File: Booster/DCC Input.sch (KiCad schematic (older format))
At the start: 17 parts, among them P201 CONN_01X02, P202 CONN_01X02, SW201 FORCE_ENABLE, U201 6N136, U203 LM339, Y701 74HC86

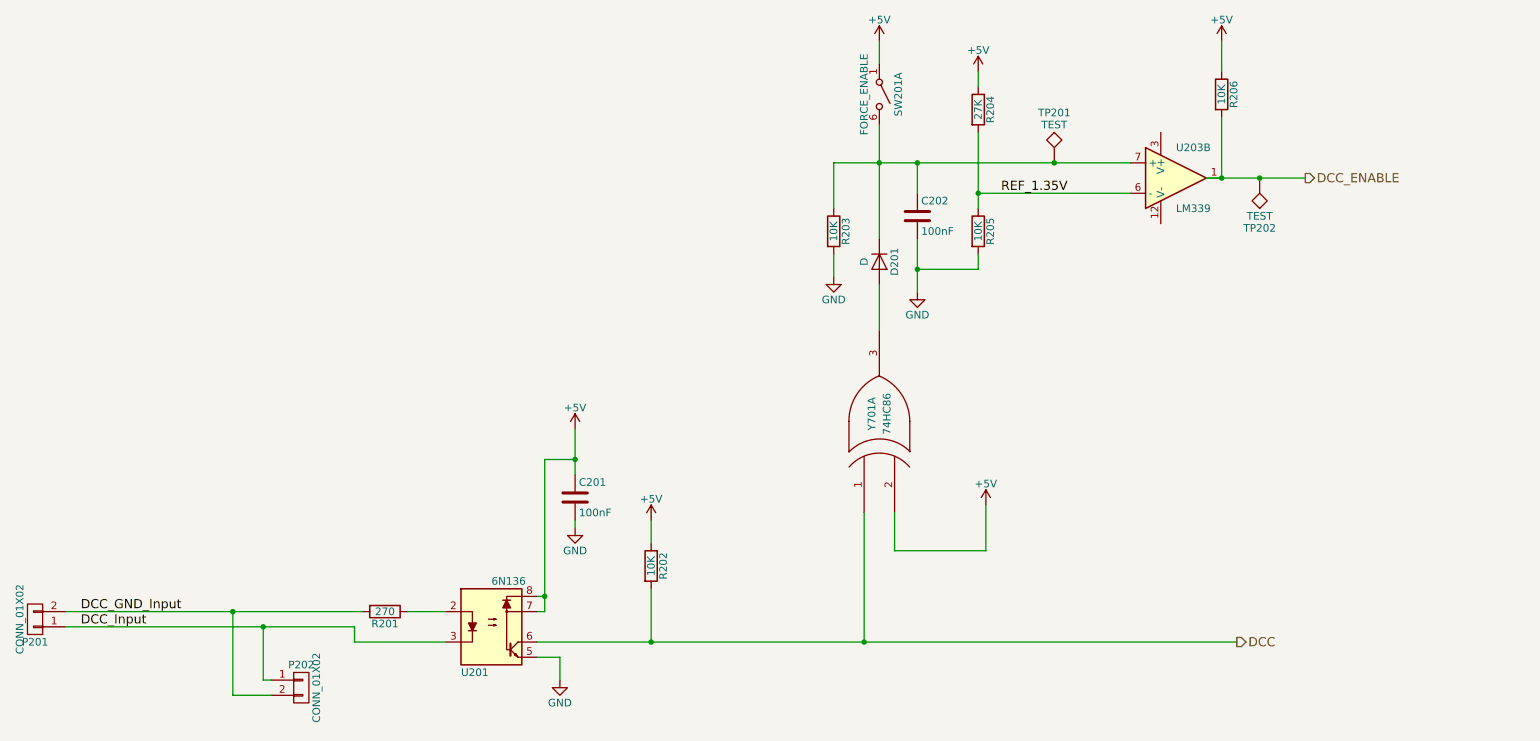
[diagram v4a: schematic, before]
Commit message: Assigned footprints & minor adjustments.
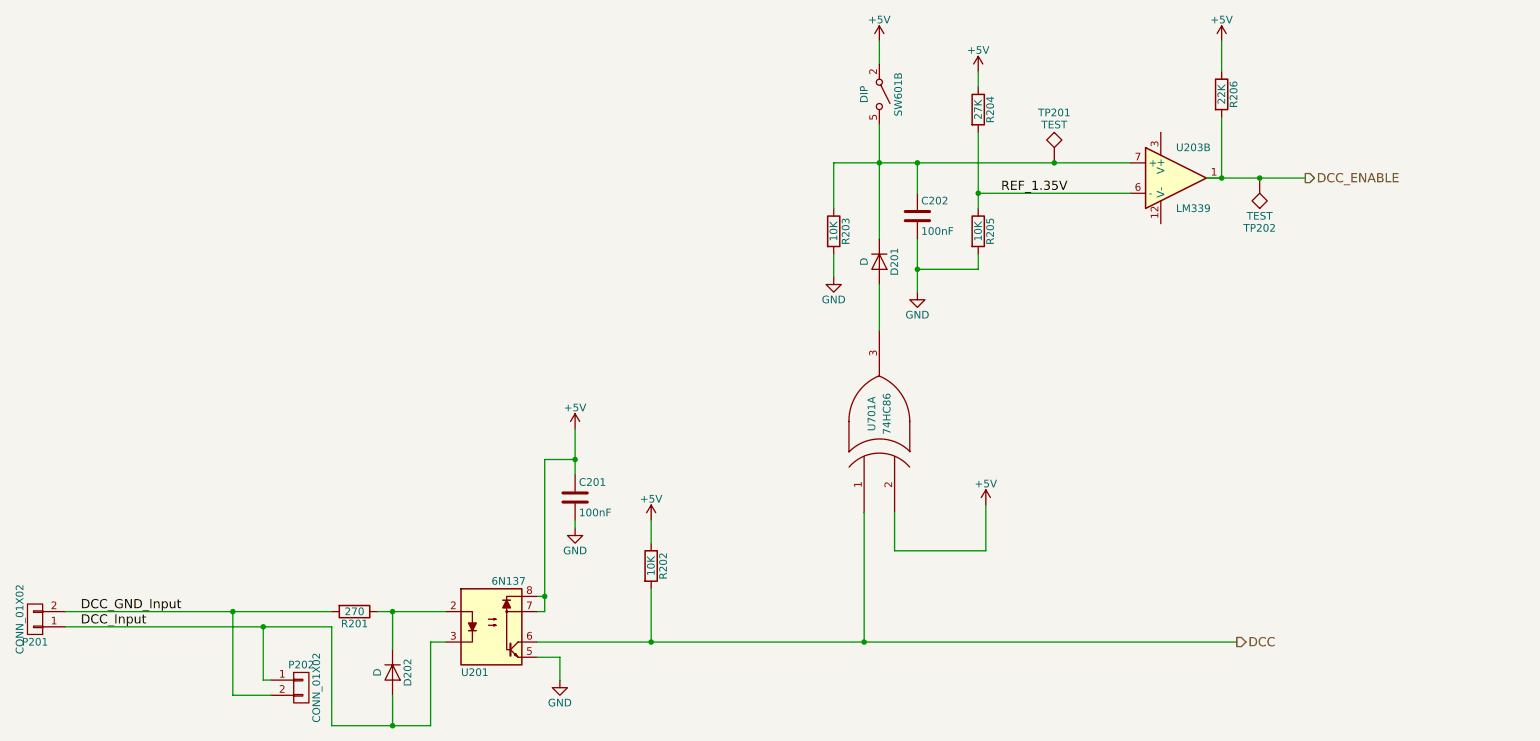
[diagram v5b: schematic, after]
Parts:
- added D202: D, Diodes_SMD:D_MiniMELF, symbol D
- C201, C202: footprint (none) -> Capacitors_SMD:C_0805
- D201: footprint (none) -> Diodes_SMD:D_MiniMELF
- P201, P202: footprint (none) -> Connectors_JST:JST_XH_B02B-XH-A_02x2.50mm_Straight
- R201, R202, R203, R204, R205: footprint (none) -> Resistors_SMD:R_0805
- R206: value 10K -> 22K; footprint (none) -> Resistors_SMD:R_0805
- SW601: renamed from SW201; value FORCE_ENABLE -> DIP; footprint (none) -> Buttons_Switches_THT:SW_DIP_x3_W7.62mm_Slide
- TP201, TP202: footprint (none) -> Measurement_Points:Measurement_Point_Round-TH_Small
- U201: value 6N136 -> 6N137
- U203: footprint (none) -> SMD_Packages:SOIC-14_N
- U701: renamed from Y701; footprint (none) -> SMD_Packages:SOIC-14_N
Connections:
- net +5V: now also SW601.2 (A); no longer SW601.1 (A)
- net DCC_Input: now also D202.2 (A)
- net at R201.1, U201.2: now also D202.1 (K)
- net at C202.1, D201.1 (K), R203.1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: now also SW601.5 (B); no longer SW601.6 (B)
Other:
- moved on the sheet: R201
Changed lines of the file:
@@
 P 4350 4900
 F 0 "U201" H 4150 4600 50  0000 L CNN
-F 1 "6N136" H 4350 5200 50  0000 L CNN
+F 1 "6N137" H 4350 5200 50  0000 L CNN
 F 2 "Housings_DIP:DIP-8_W7.62mm" H 4150 4600 50  0001 L CIN
 F 3 "" H 4350 4900 50  0001 L CNN
@@
 L R R201
 U 1 1 59E8F235
-P 3650 4800
-F 0 "R201" V 3730 4800 50  0000 C CNN
-F 1 "270" V 3650 4800 50  0000 C CNN
-F 2 "" V 3580 4800 50  0001 C CNN
-F 3 "" H 3650 4800 50  0001 C CNN
-	1    3650 4800
+P 3450 4800
+F 0 "R201" V 3530 4800 50  0000 C CNN
+F 1 "270" V 3450 4800 50  0000 C CNN
+F 2 "Resistors_SMD:R_0805" V 3380 4800 50  0001 C CNN
+F 3 "" H 3450 4800 50  0001 C CNN
+	1    3450 4800
 	0    1    1    0
 $EndComp
@@
 F 0 "C201" H 4925 4150 50  0000 L CNN
 F 1 "100nF" H 4925 3950 50  0000 L CNN
-F 2 "" H 4938 3900 50  0001 C CNN
+F 2 "Capacitors_SMD:C_0805" H 4938 3900 50  0001 C CNN
 F 3 "" H 4900 4050 50  0001 C CNN
 	1    4900 4050
@@
 F 0 "R202" V 5480 4500 50  0000 C CNN
 F 1 "10K" V 5400 4500 50  0000 C CNN
-F 2 "" V 5330 4500 50  0001 C CNN
+F 2 "Resistors_SMD:R_0805" V 5330 4500 50  0001 C CNN
 F 3 "" H 5400 4500 50  0001 C CNN
 	1    5400 4500
@@
 F 0 "D201" H 6900 2600 50  0000 C CNN
 F 1 "D" H 6900 2400 50  0000 C CNN
-F 2 "" H 6900 2500 50  0000 C CNN
+F 2 "Diodes_SMD:D_MiniMELF" H 6900 2500 50  0001 C CNN
 F 3 "" H 6900 2500 50  0000 C CNN
 	1    6900 2500
@@
 F 0 "C202" H 7175 2300 50  0000 L CNN
 F 1 "100nF" H 7175 2100 50  0000 L CNN
-F 2 "" H 7188 2050 50  0000 C CNN
+F 2 "Capacitors_SMD:C_0805" H 7188 2050 50  0001 C CNN
 F 3 "" H 7150 2200 50  0000 C CNN
 	1    7150 2200
@@
 F 0 "U203" H 8850 2150 50  0000 L CNN
 F 1 "LM339" H 8850 1750 50  0000 L CNN
-F 2 "" H 8800 2050 50  0000 C CNN
+F 2 "SMD_Packages:SOIC-14_N" H 8800 2050 50  0001 C CNN
 F 3 "" H 8900 2150 50  0000 C CNN
 	2    8850 1950
@@
 F 0 "R204" V 7630 1500 50  0000 C CNN
 F 1 "27K" V 7550 1500 50  0000 C CNN
-F 2 "" V 7480 1500 50  0000 C CNN
+F 2 "Resistors_SMD:R_0805" V 7480 1500 50  0001 C CNN
 F 3 "" H 7550 1500 50  0000 C CNN
 	1    7550 1500
@@
 F 0 "R205" V 7630 2300 50  0000 C CNN
 F 1 "10K" V 7550 2300 50  0000 C CNN
-F 2 "" V 7480 2300 50  0000 C CNN
+F 2 "Resistors_SMD:R_0805" V 7480 2300 50  0001 C CNN
 F 3 "" H 7550 2300 50  0000 C CNN
 	1    7550 2300
@@
 F 0 "R203" V 6680 2300 50  0000 C CNN
 F 1 "10K" V 6600 2300 50  0000 C CNN
-F 2 "" V 6530 2300 50  0000 C CNN
+F 2 "Resistors_SMD:R_0805" V 6530 2300 50  0001 C CNN
 F 3 "" H 6600 2300 50  0000 C CNN
 	1    6600 2300
@@
 P 9150 1400
 F 0 "R206" V 9230 1400 50  0000 C CNN
-F 1 "10K" V 9150 1400 50  0000 C CNN
-F 2 "" V 9080 1400 50  0000 C CNN
+F 1 "22K" V 9150 1400 50  0000 C CNN
+F 2 "Resistors_SMD:R_0805" V 9080 1400 50  0001 C CNN
 F 3 "" H 9150 1400 50  0000 C CNN
 	1    9150 1400
@@
 REF_1.35V
 $Comp
-L SW_SPST_x03 SW201
-U 1 1 5A38F800
+L SW_SPST_x03 SW601
+U 2 1 5A38F800
 P 6900 1400
-F 0 "SW201" H 6900 1525 50  0000 C CNN
-F 1 "FORCE_ENABLE" H 6900 1300 50  0000 C CNN
-F 2 "" H 6900 1400 50  0001 C CNN
+F 0 "SW601" H 6900 1525 50  0000 C CNN
+F 1 "DIP" H 6900 1300 50  0000 C CNN
+F 2 "Buttons_Switches_THT:SW_DIP_x3_W7.62mm_Slide" H 6900 1400 50  0001 C CNN
 F 3 "" H 6900 1400 50  0001 C CNN
-	1    6900 1400
+	2    6900 1400
 	0    1    1    0
 $EndComp
@@
 F 0 "P202" H 3100 5450 50  0000 C CNN
 F 1 "CONN_01X02" V 3200 5300 50  0000 C CNN
-F 2 "" H 3100 5300 50  0000 C CNN
+F 2 "Connectors_JST:JST_XH_B02B-XH-A_02x2.50mm_Straight" H 3100 5300 50  0001 C CNN
 F 3 "" H 3100 5300 50  0000 C CNN
 	1    3100 5300
@@
 F 0 "P201" H 1350 5000 50  0000 C CNN
 F 1 "CONN_01X02" V 1450 4850 50  0000 C CNN
-F 2 "" H 1350 4850 50  0000 C CNN
+F 2 "Connectors_JST:JST_XH_B02B-XH-A_02x2.50mm_Straight" H 1350 4850 50  0001 C CNN
 F 3 "" H 1350 4850 50  0000 C CNN
 	1    1350 4850
@@
 $EndComp
 $Comp
-L 74HC86 Y701
+L 74HC86 U701
 U 1 1 5A3AC211
 P 6900 3550
-F 0 "Y701" H 6950 3600 50  0000 C CNN
+F 0 "U701" H 6950 3600 50  0000 C CNN
 F 1 "74HC86" H 6950 3500 50  0000 C CNN
-F 2 "" H 6900 3550 50  0000 C CNN
+F 2 "SMD_Packages:SOIC-14_N" H 6900 3550 50  0001 C CNN
 F 3 "" H 6900 3550 50  0000 C CNN
 	1    6900 3550
@@
 F 0 "TP202" H 9400 2250 50  0000 C BNN
 F 1 "TEST" H 9400 2200 50  0000 C CNN
-F 2 "" H 9400 1950 50  0000 C CNN
+F 2 "Measurement_Points:Measurement_Point_Round-TH_Small" H 9400 1950 50  0001 C CNN
 F 3 "" H 9400 1950 50  0000 C CNN
 	1    9400 1950
@@
 F 0 "TP201" H 8050 2150 50  0000 C BNN
 F 1 "TEST" H 8050 2100 50  0000 C CNN
-F 2 "" H 8050 1850 50  0000 C CNN
+F 2 "Measurement_Points:Measurement_Point_Round-TH_Small" H 8050 1850 50  0001 C CNN
 F 3 "" H 8050 1850 50  0000 C CNN
 	1    8050 1850
@@
 	6900 2950 6900 2650
 Wire Wire Line
-	6800 4150 6800 5000
-Wire Wire Line
-	3800 4800 4050 4800
-Wire Wire Line
-	3450 5000 4050 5000
+	6800 5000 6800 4150
+Wire Wire Line
+	3600 4800 4050 4800
 Wire Wire Line
 	5400 4350 5400 4200
@@
 	7550 2450 7550 2550
 Wire Wire Line
-	3450 4900 3450 5000
+	3300 4900 3300 5550
 Connection ~ 6800 5000
 Connection ~ 7150 1850
@@
 	2900 5250 2850 5250
 Wire Wire Line
-	1550 4900 3450 4900
-Wire Wire Line
-	1550 4800 3500 4800
+	1550 4900 3300 4900
+Wire Wire Line
+	1550 4800 3300 4800
+$Comp
+L D D202
+U 1 1 5A411C39
+P 3700 5200
+F 0 "D202" H 3700 5300 50  0000 C CNN
+F 1 "D" H 3700 5100 50  0000 C CNN
+F 2 "Diodes_SMD:D_MiniMELF" H 3700 5200 50  0001 C CNN
+F 3 "" H 3700 5200 50  0000 C CNN
+	1    3700 5200
+	0    1    1    0
+$EndComp
+Wire Wire Line
+	3300 5550 3950 5550
+Wire Wire Line
+	3700 5550 3700 5350
+Wire Wire Line
+	3700 5050 3700 4800
+Connection ~ 3700 4800
+Wire Wire Line
+	3950 5550 3950 5000
+Wire Wire Line
+	3950 5000 4050 5000
+Connection ~ 3700 5550
 $EndSCHEMATC

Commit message: Starting to add traces. Minor schematic changes to aid routing.
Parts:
- U201: footprint Housings_DIP:DIP-8_W7.62mm -> Housings_DIP:SMDIP-8_W9.53mm_Clearance8mm
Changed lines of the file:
@@
 F 0 "U201" H 4150 4600 50  0000 L CNN
 F 1 "6N137" H 4350 5200 50  0000 L CNN
-F 2 "Housings_DIP:DIP-8_W7.62mm" H 4150 4600 50  0001 L CIN
+F 2 "Housings_DIP:SMDIP-8_W9.53mm_Clearance8mm" H 4150 4600 50  0001 L CIN
 F 3 "" H 4350 4900 50  0001 L CNN
 	1    4350 4900
@@
 $EndComp
 $Comp
-L GND #PWR01
+L GND #PWR201
 U 1 1 59E8F260
 P 4800 5250
-F 0 "#PWR01" H 4800 5000 50  0001 C CNN
+F 0 "#PWR201" H 4800 5000 50  0001 C CNN
 F 1 "GND" H 4800 5100 50  0000 C CNN
 F 2 "" H 4800 5250 50  0001 C CNN
@@
 DCC_ENABLE
 $Comp
-L +5V #PWR02
+L +5V #PWR204
 U 1 1 59E8F78D
 P 5400 4200
-F 0 "#PWR02" H 5400 4050 50  0001 C CNN
+F 0 "#PWR204" H 5400 4050 50  0001 C CNN
 F 1 "+5V" H 5400 4340 50  0000 C CNN
 F 2 "" H 5400 4200 50  0001 C CNN
@@
 $EndComp
 $Comp
-L +5V #PWR03
+L +5V #PWR208
 U 1 1 59E8F877
 P 7550 1250
-F 0 "#PWR03" H 7550 1100 50  0001 C CNN
+F 0 "#PWR208" H 7550 1100 50  0001 C CNN
 F 1 "+5V" H 7550 1390 50  0000 C CNN
 F 2 "" H 7550 1250 50  0001 C CNN
@@
 $EndComp
 $Comp
-L GND #PWR04
+L GND #PWR207
 U 1 1 5A383AD2
 P 7150 2700
-F 0 "#PWR04" H 7150 2450 50  0001 C CNN
+F 0 "#PWR207" H 7150 2450 50  0001 C CNN
 F 1 "GND" H 7150 2550 50  0000 C CNN
 F 2 "" H 7150 2700 50  0000 C CNN
@@
 $EndComp
 $Comp
-L GND #PWR05
+L GND #PWR205
 U 1 1 5A38E8FE
 P 6600 2600
-F 0 "#PWR05" H 6600 2350 50  0001 C CNN
+F 0 "#PWR205" H 6600 2350 50  0001 C CNN
 F 1 "GND" H 6600 2450 50  0000 C CNN
 F 2 "" H 6600 2600 50  0000 C CNN
@@
 $EndComp
 $Comp
-L +5V #PWR06
+L +5V #PWR210
 U 1 1 5A38EB05
 P 9150 1050
-F 0 "#PWR06" H 9150 900 50  0001 C CNN
+F 0 "#PWR210" H 9150 900 50  0001 C CNN
 F 1 "+5V" H 9150 1190 50  0000 C CNN
 F 2 "" H 9150 1050 50  0001 C CNN
@@
 $EndComp
 $Comp
-L +5V #PWR07
+L +5V #PWR206
 U 1 1 5A38FAC1
 P 6900 1050
-F 0 "#PWR07" H 6900 900 50  0001 C CNN
+F 0 "#PWR206" H 6900 900 50  0001 C CNN
 F 1 "+5V" H 6900 1190 50  0000 C CNN
 F 2 "" H 6900 1050 50  0001 C CNN
@@
 $EndComp
 $Comp
-L GND #PWR08
+L GND #PWR203
 U 1 1 5A3A1465
 P 4900 4250
-F 0 "#PWR08" H 4900 4000 50  0001 C CNN
+F 0 "#PWR203" H 4900 4000 50  0001 C CNN
 F 1 "GND" H 4900 4100 50  0000 C CNN
 F 2 "" H 4900 4250 50  0001 C CNN
@@
 $EndComp
 $Comp
-L +5V #PWR09
+L +5V #PWR202
 U 1 1 5A3A1566
 P 4900 3600
-F 0 "#PWR09" H 4900 3450 50  0001 C CNN
+F 0 "#PWR202" H 4900 3450 50  0001 C CNN
 F 1 "+5V" H 4900 3740 50  0000 C CNN
 F 2 "" H 4900 3600 50  0001 C CNN
@@
 $EndComp
 $Comp
-L +5V #PWR010
+L +5V #PWR209
 U 1 1 5A3ACB63
 P 7600 4100
-F 0 "#PWR010" H 7600 3950 50  0001 C CNN
+F 0 "#PWR209" H 7600 3950 50  0001 C CNN
 F 1 "+5V" H 7600 4240 50  0000 C CNN
 F 2 "" H 7600 4100 50  0001 C CNN

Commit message: Changed booster reversed polarity protection from a diode to a p channel mosfet to reduce the voltage drop.
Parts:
- C201: footprint Capacitors_SMD:C_0805 -> TO_SOT_Packages_THT:TO-220-2_Vertical
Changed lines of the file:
@@
 F 0 "C201" H 4925 4150 50  0000 L CNN
 F 1 "100nF" H 4925 3950 50  0000 L CNN
-F 2 "Capacitors_SMD:C_0805" H 4938 3900 50  0001 C CNN
+F 2 "TO_SOT_Packages_THT:TO-220-2_Vertical" H 4938 3900 50  0001 C CNN
 F 3 "" H 4900 4050 50  0001 C CNN
 	1    4900 4050
